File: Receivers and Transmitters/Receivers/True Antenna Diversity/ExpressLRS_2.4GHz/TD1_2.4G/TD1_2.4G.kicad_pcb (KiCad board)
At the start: 4 copper layers, 39.5 x 39.5 mm, 54 parts, among them J1 Conn_01x04_Pin, J2 Conn_01x04_Socket, U1 TPS7A4701xRGW, U2 SX1280IMLTRT, U3 SX1280IMLTRT, U4 RFX2401C, U5 2450LP14B100, U6 RFX2401C, U7 2450LP14B100, U8 ESP32-PICO-D4, Y1 52MHz, Y2 52MHz

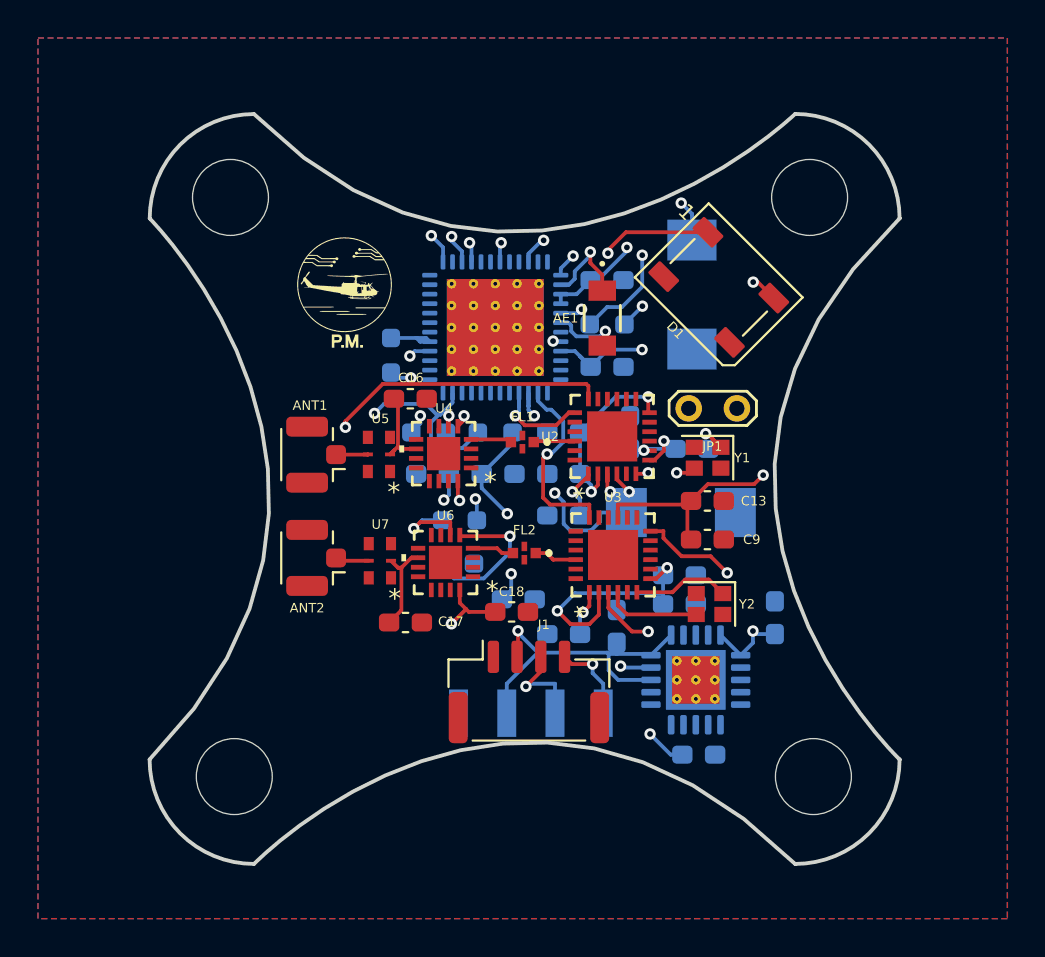
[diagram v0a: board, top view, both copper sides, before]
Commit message: Update Antenna Diversity (AD1_2.4G), True Antenna Diversity (TD1_2.4G), and Gemini Mode transmitter (G_TX1): Modify KiCad files, add BOMs and production files; update images, docs, videos, and README; remove outdated Mechanical CAD file
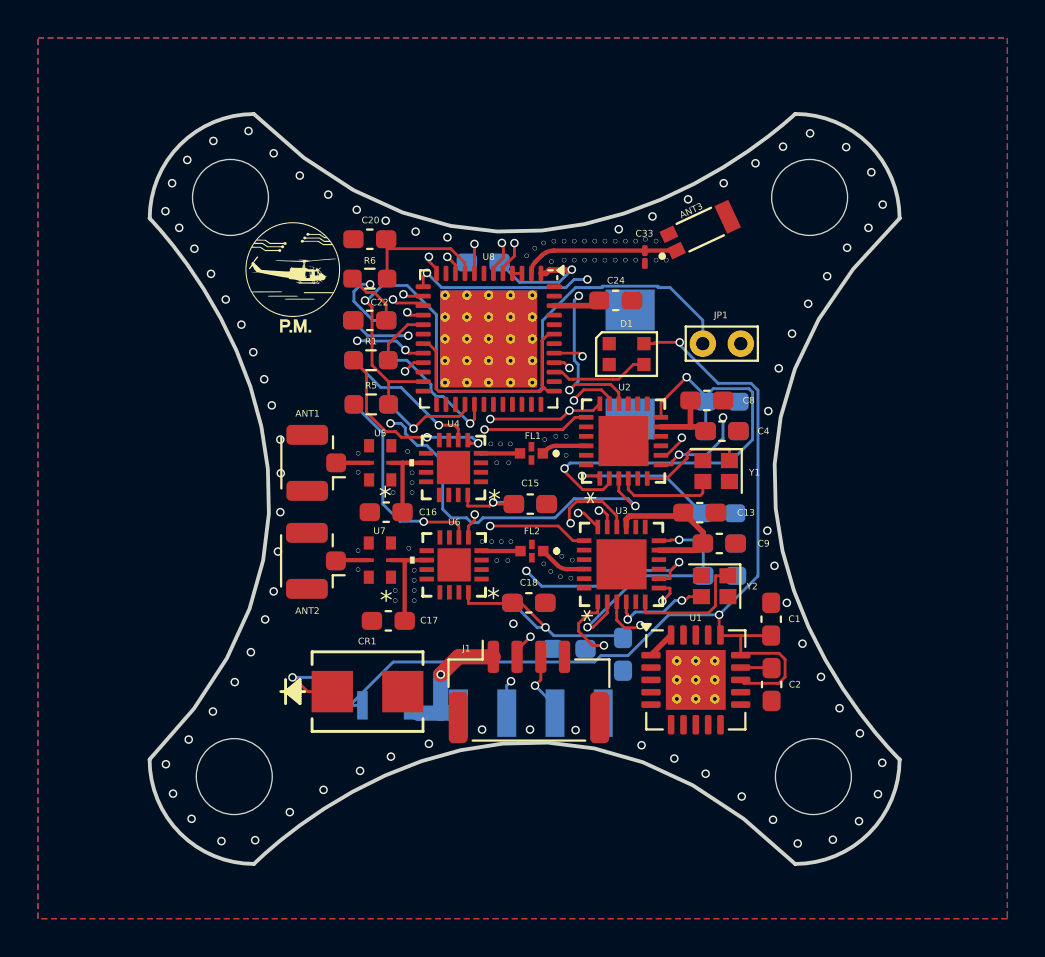
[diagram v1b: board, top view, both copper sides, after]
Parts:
- removed AE1: W3008, W3008:ANT_W3008_PUL
- removed C21: 10uF, ECASD40J106M055K00:ECASD40J106M055K00
- removed REF**: OSHW-Logo_5.7x6mm_SilkScreen, Symbol:OSHW-Logo_5.7x6mm_SilkScreen
- added ANT3: W3008, W3008:ANTENNA_W3008, F.Cu at (156.2, 73.7)
- added C24: 100nF, Capacitor_SMD:C_0603_1608Metric_Pad1.08x0.95mm_HandSolder, F.Cu at (151.8, 77.4)
- added C25: 100nF, Capacitor_SMD:C_0603_1608Metric_Pad1.08x0.95mm_HandSolder, B.Cu at (144.8, 75.4)
- added C33: 1.5pF, Capacitor_SMD:C_01005_0402Metric_Pad0.57x0.30mm_HandSolder, F.Cu at (153.3, 75.1)
- added CR1: SMBJ60A, ul_SMBJ60A:SMBJSeries_LTF, F.Cu at (138.7, 98.0)
- added F1: MF-PSMF020X-2, ul_MF-PSMF020X-2:FUSE_F020X_BRN, B.Cu at (139.7, 98.8)
- added QR*****: qrCode, qrlogo:qrCode, B.Cu at (137.2, 93.5)
- C1, C15, C2, C20, C22, C4, C8, R1, R5, R6, U1, U8: moved to F.Cu
- D1: value WS2812B -> WS2812B-2020; footprint LED_SMD:LED_WS2812B_PLCC4_5.0x5.0mm_P3.2mm -> LED_SMD:LED_WS2812B-2020_PLCC4_2.0x2.0mm
- JP1: value Jumper_2_Bridged -> Jumper_2_Small_Bridged; footprint TestPoint:TestPoint_2Pads_Pitch2.54mm_Drill0.8mm -> TestPoint:TestPoint_Bridge_Pitch2.0mm_Drill0.7mm
- moved C20 14.2 mm to (138.8, 74.2), turned to 0 degrees
- moved R3 13.6 mm to (138.8, 78.5)
- moved R6 12.7 mm to (138.8, 76.3), turned to 0 degrees
- moved C22 12.7 mm to (138.8, 78.5), turned to 180 degrees
- moved C7 9.17 mm to (157.4, 82.8), turned to 0 degrees
- moved C6 8.34 mm to (157.4, 84.3), turned to 0 degrees
- moved C3 8.23 mm to (152.2, 96.1), turned to -90 degrees
- moved C5 8.17 mm to (157.2, 88.6), turned to 180 degrees
- moved C1 8.14 mm to (160.0, 94.2)
- moved R4 7.67 mm to (138.9, 82.9)
- moved R5 6.70 mm to (138.9, 82.9), turned to 0 degrees
- moved C16 6.11 mm to (139.7, 88.6), turned to 180 degrees
- moved D1 5.99 mm to (152.4, 80.2), turned to 0 degrees
- moved C14 5.39 mm to (147.3, 88.2), turned to 0 degrees
- moved C2 5.33 mm to (160.0, 97.7), turned to -90 degrees
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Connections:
- C1 pad 1: +5V -> F2
- D1 pad 1: +5V -> unconnected-(D1-DOUT-Pad1)
- D1 pad 2: unconnected-(D1-DOUT-Pad2) -> GND
- D1 pad 3: GND -> Net-(D1-DIN)
- D1 pad 4: Net-(D1-DIN) -> F2
- J1 pad 1: GND -> +5V
- J1 pad 2: +5V -> /TX
- J1 pad 3: /TX -> /RX
- J1 pad 4: /RX -> GND
- J2 pad 1: GND -> +5V
- J2 pad 2: +5V -> /TX
- J2 pad 3: /TX -> /RX
- J2 pad 4: /RX -> GND
- JP1 pad 1: Net-(JP1-A) -> GND
- U1 pad 13: +5V -> F2
- U1 pad 15: +5V -> F2
- U1 pad 16: +5V -> F2
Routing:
- net F2: track 0.00 -> 58.6 mm, vias 0 -> 3
- net +5V: track 45.9 -> 8.25 mm, vias 2 -> 1
- net /MISO: track 0.00 -> 33.5 mm, vias 0 -> 5
- net /ESP32/DIO2: track 0.00 -> 30.0 mm, vias 0 -> 3
- net /MOSI: track 0.00 -> 25.5 mm, vias 0 -> 3
- net Net-(U8-EN): track 32.0 -> 7.06 mm, vias 3 -> 0
- net /ESP32/NSS_CTS_2: track 0.00 -> 24.8 mm, vias 0 -> 3
- net /TX: track 5.03 -> 26.1 mm, vias 1 -> 3
- net /ESP32/TXEN_2: track 0.00 -> 17.2 mm, vias 0 -> 2
- net Net-(D1-DIN): track 20.8 -> 5.21 mm, vias 2 -> 0
- net /RESET: track 21.3 -> 36.6 mm, vias 3 -> 4
- net /SX1280_ANT1/VDD_INN: track 9.99 -> 25.0 mm
- net /SX1280_ANT2/VDD_INN: track 26.3 -> 13.3 mm
- net /BUSY_1: track 11.4 -> 23.2 mm, vias 2 -> 3
- net /BUSY_2: track 16.0 -> 27.4 mm
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- added copper zone on In3.Cu, net GND
- added copper zone on In4.Cu, net GND
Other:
- copper layers 4 -> 6
- board text added: "TD1_2.4GHz TRUE DIVERSITY RX Board (Gemini Mode Compatible) REV: 1.0 2025-02-23"

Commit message: Update TD1_2.4G: schematic and PCB revisions, BOM export, README; remove old PCBWay production files
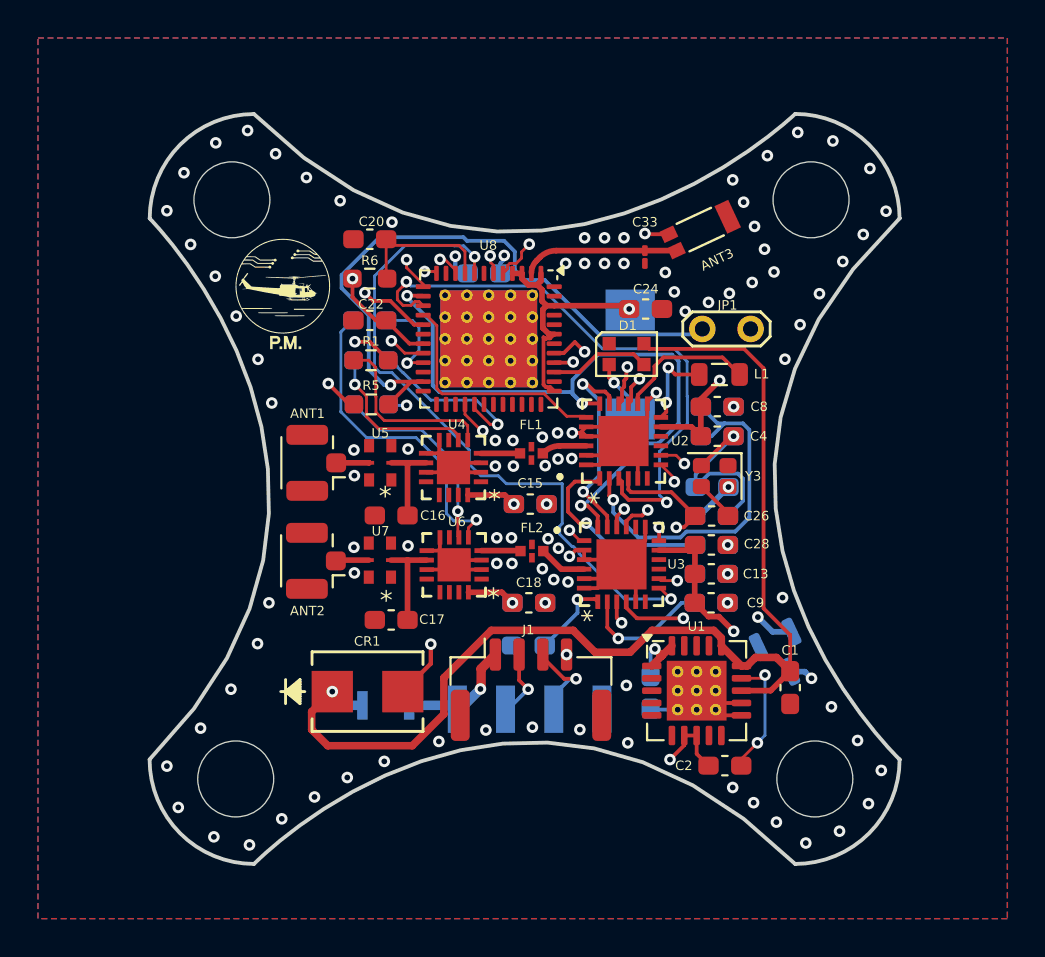
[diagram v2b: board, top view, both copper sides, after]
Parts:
- removed QR*****: qrCode, qrlogo:qrCode
- removed Y1, Y2: 52MHz, Crystal:Crystal_SMD_2016-4Pin_2.0x1.6mm
- removed hole3: , 
- removed hole4: MountingHole_4mm, MountingHole:MountingHole_4mm
- added C26: 1nF, Capacitor_SMD:C_0603_1608Metric_Pad1.08x0.95mm_HandSolder, F.Cu at (156.8, 88.8)
- added C27: 100nF, Capacitor_SMD:C_0603_1608Metric_Pad1.08x0.95mm_HandSolder, B.Cu at (156.8, 88.8)
- added C28: 1uF, Capacitor_SMD:C_0603_1608Metric_Pad1.08x0.95mm_HandSolder, F.Cu at (156.8, 90.3)
- added C29: 1uF, Capacitor_SMD:C_0603_1608Metric_Pad1.08x0.95mm_HandSolder, B.Cu at (156.9, 87.2)
- added G***: LOGO, LOGO, B.Cu at (139.7, 87.7)
- added Hole3: , , F.Cu at (131.8, 102.6)
- added Hole4: , , F.Cu at (162.3, 102.6)
- added L1: 15u, Inductor_SMD:L_0805_2012Metric, F.Cu at (157.2, 81.3)
- added U11: AP2138N-2.8TRG1, Package_TO_SOT_SMD:SOT-23, B.Cu at (160.6, 96.1)
- added Y3: 52Mhz TCXO, Crystal:Crystal_SMD_2016-4Pin_2.0x1.6mm, F.Cu at (157.0, 86.7)
- JP1: footprint TestPoint:TestPoint_Bridge_Pitch2.0mm_Drill0.7mm -> TestPoint:TestPoint_2Pads_Pitch2.54mm_Drill0.8mm
- hole1: value MountingHole_4mm -> (none); footprint MountingHole:MountingHole_4mm -> (none)
- moved C2 4.93 mm to (157.5, 101.9), turned to 180 degrees
- moved C1 3.74 mm to (161.0, 97.8), turned to -90 degrees
- moved C13 3.28 mm to (156.8, 91.8)
- moved C9 3.15 mm to (156.8, 93.3)
- moved C3 2.47 mm to (153.6, 98.1)
- moved C10 2.16 mm to (147.2, 95.6)
- moved C5 1.71 mm to (156.8, 90.3)
- moved C12 1.65 mm to (156.8, 91.8)
- moved C24 1.64 mm to (153.4, 77.9)
- moved C11 1.49 mm to (156.8, 93.3)
- moved G*** 1.02 mm to (134.2, 77.1)
- moved JP1 0.78 mm to (156.3, 78.9)
- moved C8 0.64 mm to (157.1, 83.0)
- moved C25 0.58 mm to (144.8, 76.0)
- moved U1 0.57 mm to (156.1, 98.0)
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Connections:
- JP1 pad 1: GND -> Net-(JP1-A)
- U2 pad 14: unconnected-(U2-DCC_SW-Pad14) -> /SX1280_ANT1/V_DCC2
- U2 pad 4: Net-(U2-XTA) -> /TCXO
- U2 pad 6: Net-(U2-XTB) -> unconnected-(U2-XTB-Pad6)
- U3 pad 4: Net-(U3-XTA) -> /TCXO
- U3 pad 6: Net-(U3-XTB) -> unconnected-(U3-XTB-Pad6)
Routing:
- net GND: track 0.00 -> 75.3 mm, vias 141 -> 109
- net /TCXO: track 0.00 -> 17.1 mm, vias 0 -> 2
- net /ESP32/DIO2: track 30.0 -> 45.3 mm, vias 3 -> 2
- net /ESP32/TXEN_2: track 17.2 -> 4.84 mm, vias 2 -> 1
- net +2.8V: track 0.00 -> 12.0 mm, vias 0 -> 2
- net /SCK: track 24.8 -> 35.2 mm, vias 4 -> 3
- net /BUSY_2: track 27.4 -> 35.6 mm
- net /SX1280_ANT1/V_DCC2: track 0.00 -> 7.38 mm
- net Net-(U3-XTB): track 6.68 -> 0.00 mm
- net /ESP32/NSS_CTS_2: track 24.8 -> 18.6 mm, vias 3 -> 2
- net Net-(U2-XTB): track 5.71 -> 0.00 mm
- net /ESP32/TXEN_1: track 3.12 -> 8.78 mm, vias 0 -> 2
- net Net-(U3-XTA): track 5.34 -> 0.00 mm, vias 2 -> 0
- net Net-(U2-XTA): track 5.30 -> 0.00 mm
- net +3.3V: track 54.4 -> 49.2 mm, vias 3 -> 12
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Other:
- board text added: "TD1_2.4GHz TRUE DIVERSITY RX Board (Gemini Mode Compatible) REV: 1.0 2025-08-28"
- board text removed: "TD1_2.4GHz TRUE DIVERSITY RX Board (Gemini Mode Compatible) REV: 1.0 2025-02-23"
